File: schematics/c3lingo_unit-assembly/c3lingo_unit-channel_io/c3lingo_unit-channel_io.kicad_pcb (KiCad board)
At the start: 2 copper layers, 75 x 45 mm, 41 parts, among them J601 Mic X In, J602 Headphone X, J603 Interconnect, U601 NE5534, U602 TPA6111A2

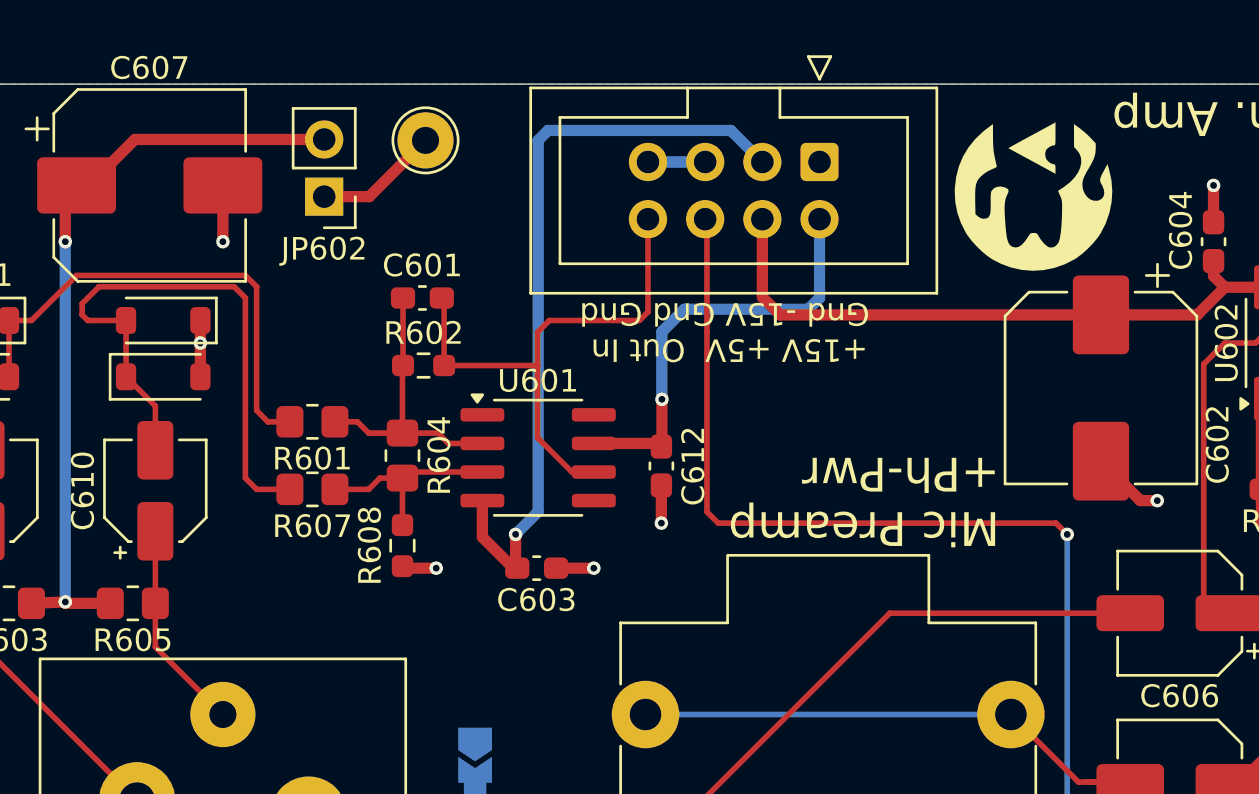
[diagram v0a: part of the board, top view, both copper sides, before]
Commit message: Channel-IO: Use horizontal IDC connector
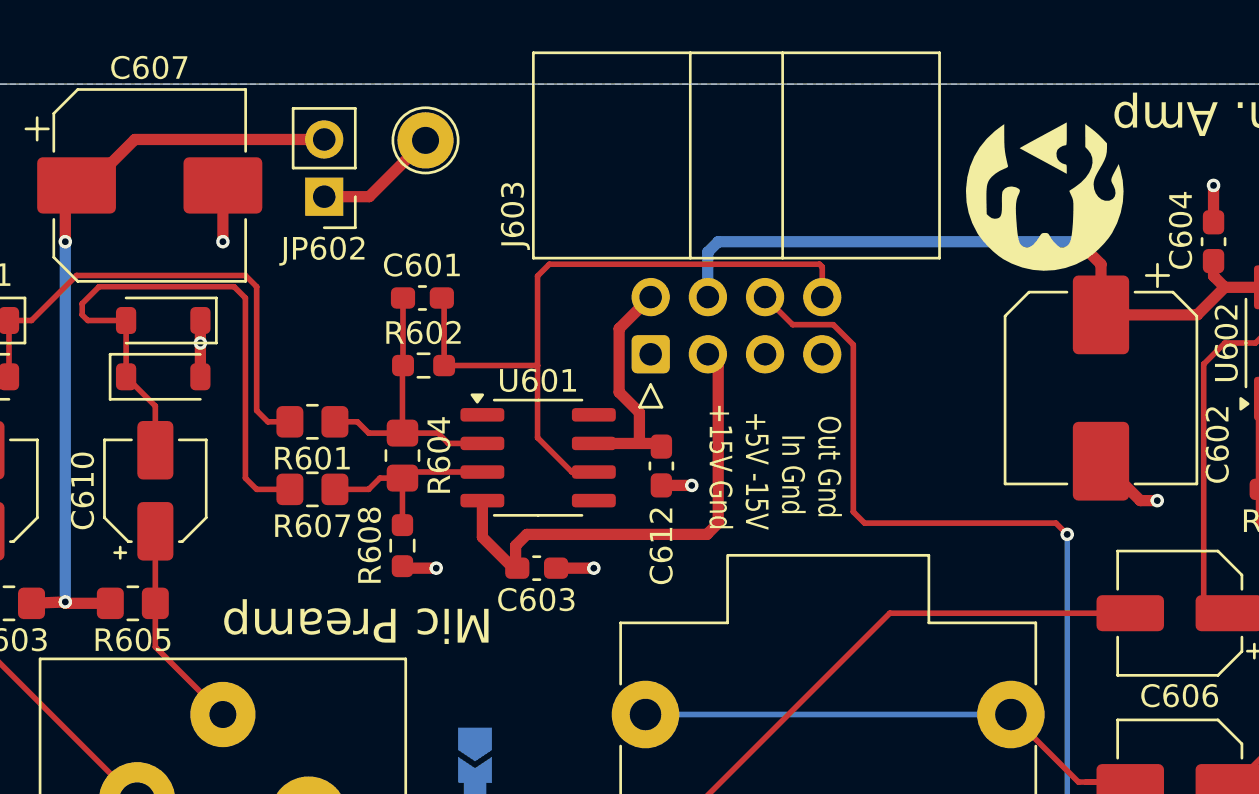
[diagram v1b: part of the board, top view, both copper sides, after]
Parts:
- J603: footprint Connector_IDC:IDC-Header_2x04_P2.54mm_Vertical -> Connector_IDC:IDC-Header_2x04_P2.54mm_Horizontal
- moved J603 11.4 mm to (84.0, 167.0), turned to 90 degrees
- moved G*** 0.50 mm to (101.5, 160.0)
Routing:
- net -15V: track 33.7 -> 21.7 mm, vias 1 -> 0
- net +15V: track 19.1 -> 10.5 mm, vias 1 -> 0
- net /Headphone: track 68.6 -> 61.2 mm
- net /MicPre: track 24.3 -> 31.6 mm
- net +5V: track 27.8 -> 31.3 mm, vias 0 -> 1
- net GND: track 30.2 -> 27.5 mm
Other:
- board text added: "Mic Preamp"
- board text added: "Out Gnd In Gnd +5V -15V +15V Gnd"
- board text added: "c3lingo Interpreter Unit Channel I/O v0.5.0-dev 2025-09-29"
- board text removed: "+15V +5V Out In Gnd -15V Gnd Gnd"
- board text removed: "Mic Preamp +Ph-Pwr"
- board text removed: "c3lingo Interpreter Unit Channel I/O v0.4.0 2025-08-26"

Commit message: Channel: Swap mic and headphone signal on IDC connector
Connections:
- J603 pad 6: /Headphone -> /MicPre
- J603 pad 8: /MicPre -> /Headphone
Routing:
- net /MicPre: track 31.6 -> 28.8 mm
- net /Headphone: track 61.2 -> 59.1 mm
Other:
- board text added: "In Gnd Out Gnd +5V -15V +15V Gnd"
- board text removed: "Out Gnd In Gnd +5V -15V +15V Gnd"
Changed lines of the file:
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@@
 			(layers "*.Cu" "*.Mask")
 			(remove_unused_layers no)
-			(net 20 "/Headphone")
+			(net 21 "/MicPre")
 			(pinfunction "Pin_6")
 			(pintype "passive")
@@
 			(layers "*.Cu" "*.Mask")
 			(remove_unused_layers no)
-			(net 21 "/MicPre")
+			(net 20 "/Headphone")
 			(pinfunction "Pin_8")
 			(pintype "passive")
@@
 		)
 	)
-	(gr_text "Out Gnd\n  In Gnd\n +5V -15V\n+15V Gnd  "
+	(gr_text "  In Gnd\nOut Gnd\n +5V -15V\n+15V Gnd  "
 		(at 89.5 172 270)
 		(layer "F.SilkS")
@@
 	)
 	(segment
-		(start 92.110537 165.686)
-		(end 93 166.575463)
+		(start 93 165.84)
+		(end 91.62 164.46)
 		(width 0.25)
 		(layer "F.Cu")
@@
 	)
 	(segment
-		(start 93 166.575463)
-		(end 93 174)
-		(width 0.25)
-		(layer "F.Cu")
-		(net 20)
-	)
-	(segment
 		(start 104.675 199.175)
 		(end 102.5 197)
@@
 	)
 	(segment
-		(start 89.08 164.46)
-		(end 90.306 165.686)
-		(width 0.25)
-		(layer "F.Cu")
-		(net 20)
-	)
-	(segment
 		(start 102.5 197)
 		(end 102.5 192)
@@
 	)
 	(segment
-		(start 90.306 165.686)
-		(end 92.110537 165.686)
+		(start 93.5 174.5)
+		(end 93 174)
 		(width 0.25)
 		(layer "F.Cu")
@@
 	)
 	(segment
-		(start 93 174)
+		(start 102 174.5)
 		(end 93.5 174.5)
 		(width 0.25)
@@
 	)
 	(segment
-		(start 102 174.5)
-		(end 93.5 174.5)
+		(start 93 174)
+		(end 93 165.84)
 		(width 0.25)
 		(layer "F.Cu")
@@
 	)
 	(segment
+		(start 89.08 164.46)
+		(end 89.08 163.58)
+		(width 0.25)
+		(layer "F.Cu")
+		(net 21)
+	)
+	(segment
 		(start 78.975 170.704999)
 		(end 78.975 167.5)
@@
 	)
 	(segment
-		(start 91.62 163.12)
-		(end 91.62 164.46)
-		(width 0.25)
-		(layer "F.Cu")
-		(net 21)
-	)
-	(segment
 		(start 81.475 172.23)
 		(end 80.500001 172.23)
@@
 	)
 	(segment
-		(start 91.5 163)
-		(end 91.62 163.12)
+		(start 89.08 163.58)
+		(end 88.5 163)
 		(width 0.25)
 		(layer "F.Cu")
@@
 	(segment
 		(start 79.5 163)
-		(end 91.5 163)
+		(end 88.5 163)
 		(width 0.25)
 		(layer "F.Cu")

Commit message: Add some artwork to the PCBs
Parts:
- added G***: LOGO, c3lingo_unit-footprints:chaosknoten-10mm, B.Cu at (104.5, 174.5)
- added G***: LOGO, c3lingo_unit-footprints:antifa-10mm, B.Cu at (71.0, 176.0)
- added REF**: OSHW-Logo_14.6x12mm_SilkScreen, Symbol:OSHW-Logo_7.5x8mm_SilkScreen, B.Cu at (63.0, 160.5)
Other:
- board text added: "Ph. Pwr (opt)"
- board text added: "c3lingo Interpreter Unit Channel I/O v1.0.0 2025-10-16"
- board text removed: "c3lingo Interpreter Unit Channel I/O v0.5.0-dev 2025-09-29"

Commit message: PCBs: Add placeholder for serial 2D barcode
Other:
- board text added: "c3lingo Interpreter Unit Channel I/O v1.0.1 2025-10-29"
- board text removed: "c3lingo Interpreter Unit Channel I/O v1.0.0 2025-10-16"
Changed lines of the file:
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@@
 	(title_block
 		(title "c3lingo interpeter unit -- channel I/O")
-		(date "2025-10-16")
-		(rev "v1.0.0")
+		(date "2025-10-29")
+		(rev "v1.0.1")
 		(company "c3lingo/ c3voc: jtbx and collaborators")
 	)
@@
 		(embedded_fonts no)
 	)
+	(gr_rect
+		(start 51 188)
+		(end 59 196)
+		(stroke
+			(width 0.12)
+			(type solid)
+		)
+		(fill yes)
+		(layer "B.SilkS")
+	)
 	(gr_line
 		(start 125 200)
@@
 		)
 	)
-	(gr_text "c3lingo Interpreter Unit\nChannel I/O\nv1.0.0 2025-10-16"
+	(gr_text "c3lingo Interpreter Unit\nChannel I/O\nv1.0.1 2025-10-29"
 		(at 88.5 159 180)
 		(layer "B.SilkS")
